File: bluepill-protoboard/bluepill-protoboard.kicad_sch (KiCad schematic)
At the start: 15 parts, among them J1 Conn_01x20_Socket, J10 Conn_01x04_Pin, J11 Conn_01x04_Pin, J13 Conn_01x06_Pin, J14 Conn_01x04_Pin, J15 Conn_01x04_Pin, J2 Conn_01x17_Pin, J3 Conn_01x17_Pin, J4 Conn_01x17_Pin, J5 Conn_01x04_Pin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

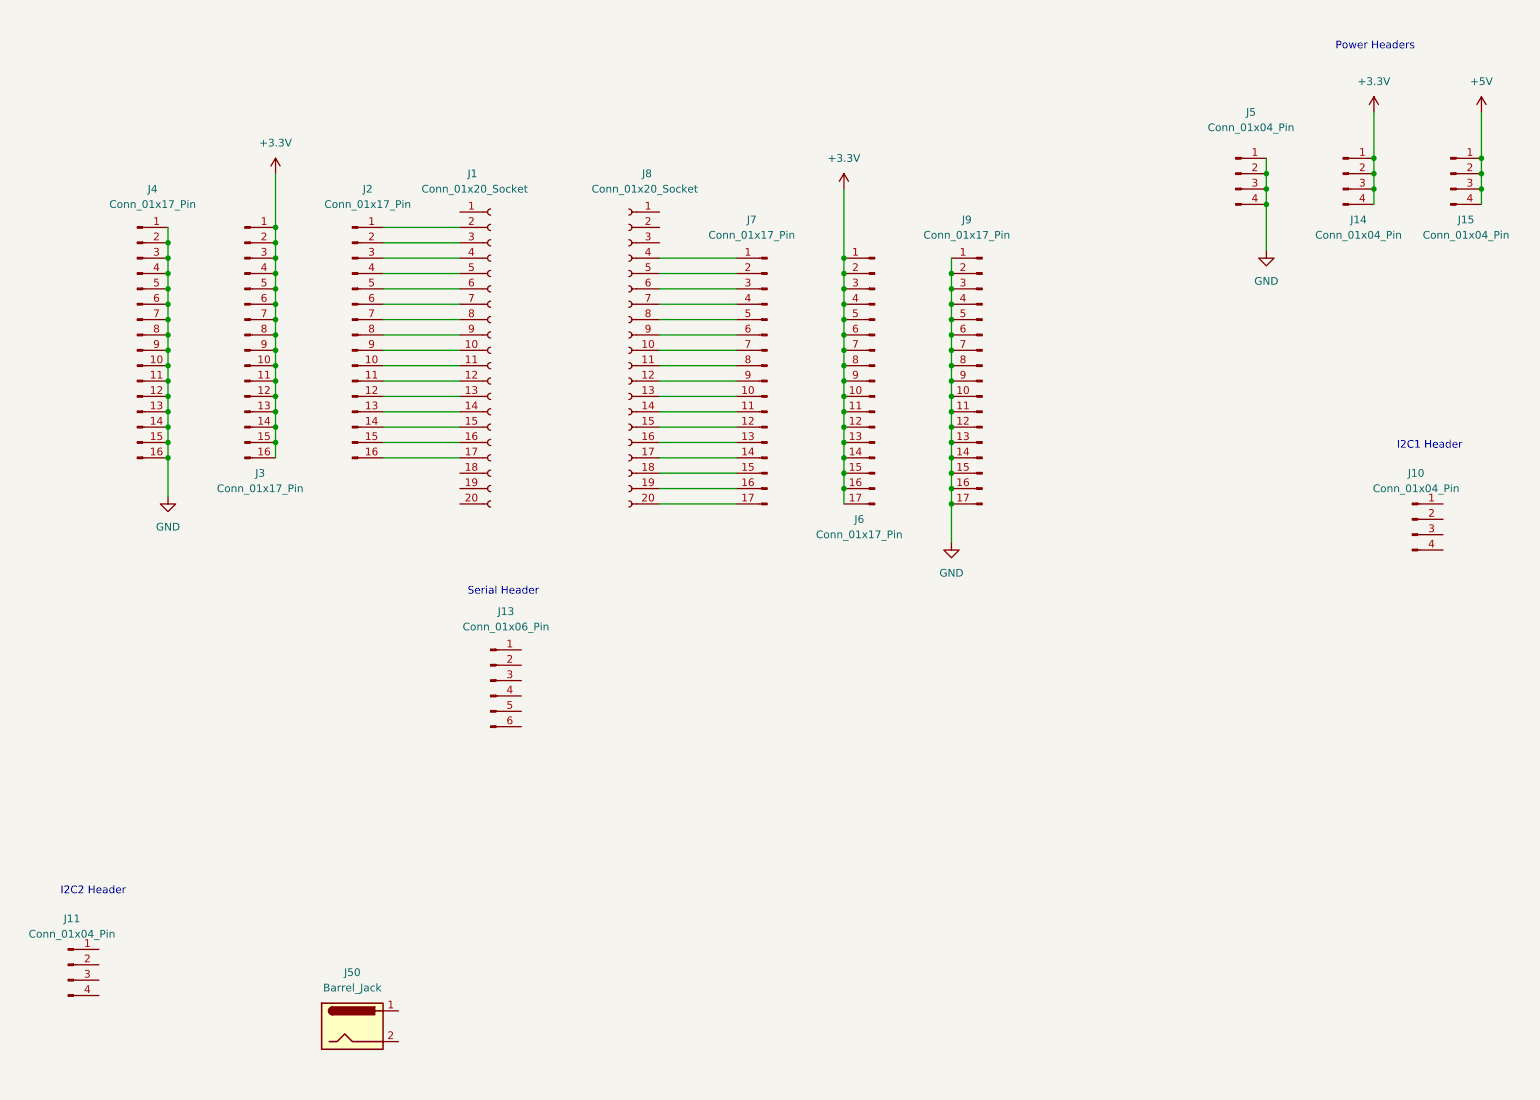
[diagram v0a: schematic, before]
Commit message: Headers done
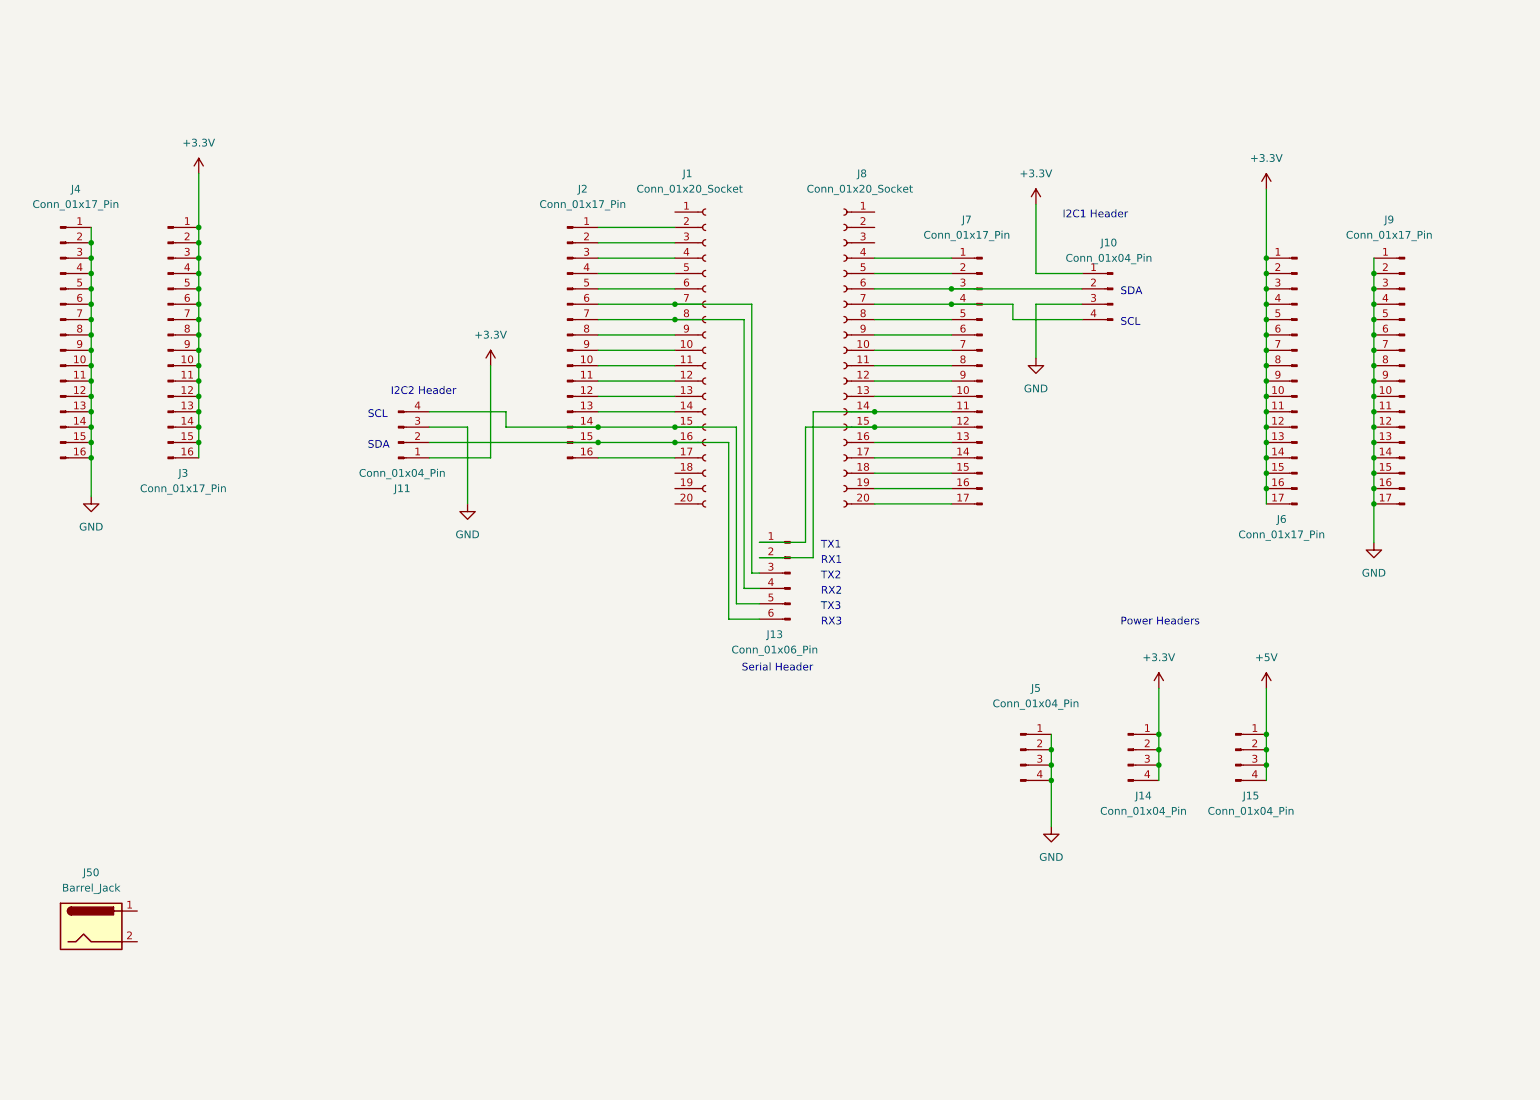
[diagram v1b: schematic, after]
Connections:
- net +3.3V: now also J10.1 (Pin_1), J11.1 (Pin_1)
- net GND: now also J10.3 (Pin_3), J11.3 (Pin_3)
- net at J1.15 (Pin_15), J2.14 (Pin_14): now also J11.4 (Pin_4), J13.5 (Pin_5)
- net at J1.16 (Pin_16), J2.15 (Pin_15): now also J11.2 (Pin_2), J13.6 (Pin_6)
- net at J1.7 (Pin_7), J2.6 (Pin_6): now also J13.3 (Pin_3)
- net at J1.8 (Pin_8), J2.7 (Pin_7): now also J13.4 (Pin_4)
- net at J10.2 (Pin_2): now also J7.3 (Pin_3), J8.6 (Pin_6)
- net at J10.4 (Pin_4): now also J7.4 (Pin_4), J8.7 (Pin_7)
- net at J7.11 (Pin_11), J8.14 (Pin_14): now also J13.2 (Pin_2)
- net at J7.12 (Pin_12), J8.15 (Pin_15): now also J13.1 (Pin_1)
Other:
- note added: "RX1"
- note added: "RX2"
- note added: "RX3"
- note added: "SCL"
- note added: "SDA"
- note added: "TX1"
- note added: "TX2"
- note added: "TX3"
- title: (none) -> Bluepill Protoboard
- moved on the sheet: J1, J10, J11, J13, J14, J15, J2, J3, J4, J5, J50, J6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

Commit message: Add license
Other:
- note added: "Licensed under GPL 3.0"
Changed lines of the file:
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@@
     (stroke (width 0) (type default))
+  )
+  (text "Licensed under GPL 3.0" (at 179.07 170.18 0)
+    (effects (font (size 1.27 1.27)) (justify left bottom))
   )
   (text "TX1" (at 152.4 102.87 0)

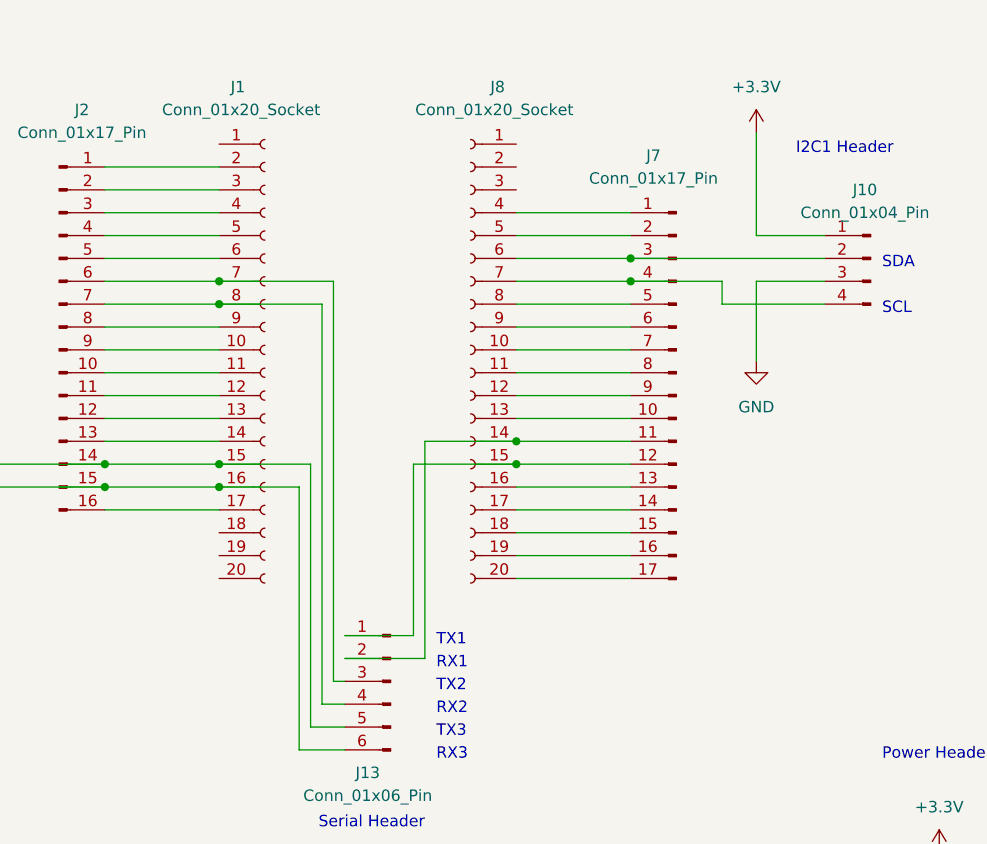
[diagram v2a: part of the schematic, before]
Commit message: Add pin labels
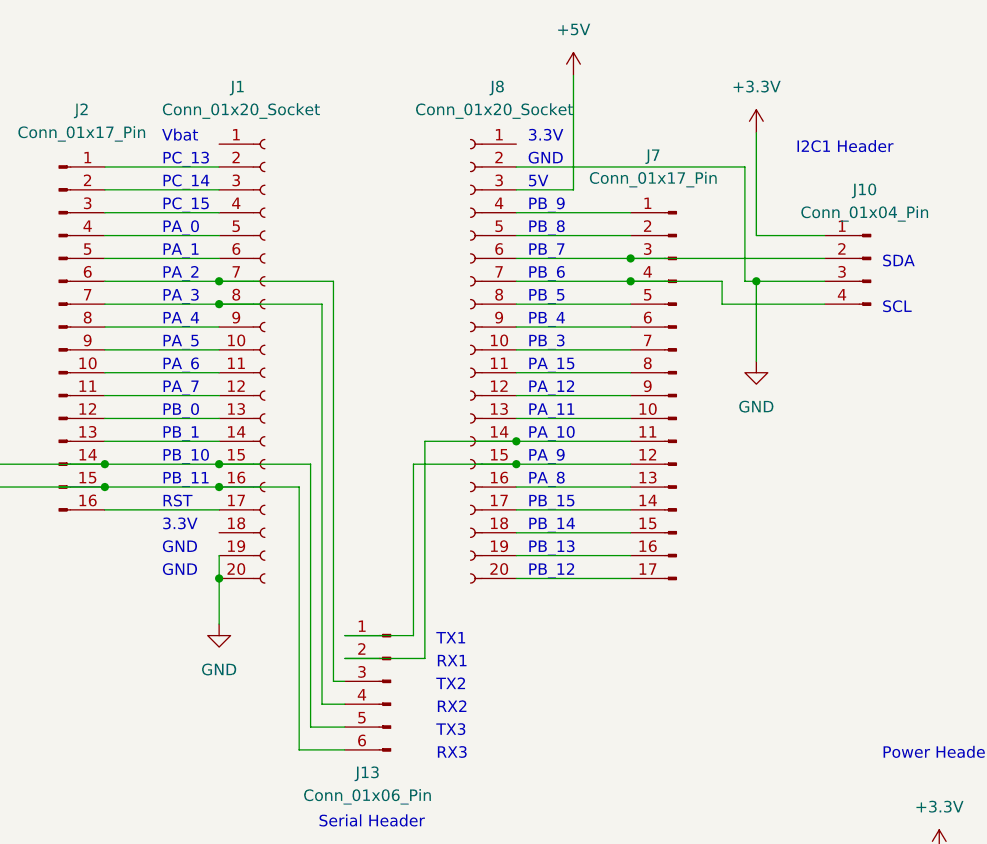
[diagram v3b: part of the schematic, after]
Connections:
- net +5V: now also J8.3 (Pin_3)
- net GND: now also J1.19 (Pin_19), J1.20 (Pin_20), J8.2 (Pin_2)
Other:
- note added: "3.3V"
- note added: "5V"
- note added: "GND"
- note added: "PA_0"
- note added: "PA_1"
- note added: "PA_10"
- note added: "PA_11"
- note added: "PA_12"
- note added: "PA_15"
- note added: "PA_2"
- note added: "PA_3"
- note added: "PA_4"
- note added: "PA_5"
- note added: "PA_6"
- note added: "PA_7"
- note added: "PA_8"
- note added: "PA_9"
- note added: "PB_0"
- note added: "PB_1"
- note added: "PB_10"
- note added: "PB_11"
- note added: "PB_12"
- note added: "PB_13"
- note added: "PB_14"
- note added: "PB_15"
- note added: "PB_3"
- note added: "PB_4"
- note added: "PB_5"
- note added: "PB_6"
- note added: "PB_7"
- note added: "PB_8"
- note added: "PB_9"
- note added: "PC_13"
- note added: "PC_14"
- note added: "PC_15"
- note added: "RST"
- note added: "Vbat"
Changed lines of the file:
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@@
   (junction (at 243.84 57.15) (diameter 0) (color 0 0 0 0)
   )
+  (junction (at 128.27 95.25) (diameter 0) (color 0 0 0 0)
+  )
   (junction (at 226.06 80.01) (diameter 0) (color 0 0 0 0)
   )
@@
   (junction (at 226.06 69.85) (diameter 0) (color 0 0 0 0)
   )
+  (junction (at 187.96 62.23) (diameter 0) (color 0 0 0 0)
+  )
   (junction (at 243.84 62.23) (diameter 0) (color 0 0 0 0)
   )
@@
     (stroke (width 0) (type default))
   )
+  (wire (pts (xy 187.96 62.23) (xy 195.58 62.23))
+    (stroke (width 0) (type default))
+  )
   (wire (pts (xy 31.75 77.47) (xy 31.75 80.01))
     (stroke (width 0) (type default))
@@
     (stroke (width 0) (type default))
   )
+  (wire (pts (xy 161.29 49.53) (xy 186.69 49.53))
+    (stroke (width 0) (type default))
+  )
   (wire (pts (xy 49.53 74.93) (xy 49.53 77.47))
     (stroke (width 0) (type default))
@@
     (stroke (width 0) (type default))
   )
+  (wire (pts (xy 128.27 95.25) (xy 128.27 100.33))
+    (stroke (width 0) (type default))
+  )
   (wire (pts (xy 149.86 82.55) (xy 161.29 82.55))
     (stroke (width 0) (type default))
@@
     (stroke (width 0) (type default))
   )
+  (wire (pts (xy 186.69 49.53) (xy 186.69 62.23))
+    (stroke (width 0) (type default))
+  )
   (wire (pts (xy 49.53 64.77) (xy 49.53 67.31))
     (stroke (width 0) (type default))
@@
     (stroke (width 0) (type default))
   )
+  (wire (pts (xy 161.29 52.07) (xy 167.64 52.07))
+    (stroke (width 0) (type default))
+  )
   (wire (pts (xy 31.75 62.23) (xy 31.75 64.77))
     (stroke (width 0) (type default))
@@
     (stroke (width 0) (type default))
   )
+  (wire (pts (xy 167.64 52.07) (xy 167.64 39.37))
+    (stroke (width 0) (type default))
+  )
   (wire (pts (xy 243.84 90.17) (xy 243.84 92.71))
     (stroke (width 0) (type default))
@@
     (stroke (width 0) (type default))
   )
-  (wire (pts (xy 195.58 62.23) (xy 187.96 62.23))
+  (wire (pts (xy 186.69 62.23) (xy 187.96 62.23))
     (stroke (width 0) (type default))
   )
@@
     (stroke (width 0) (type default))
   )
+  (wire (pts (xy 128.27 92.71) (xy 128.27 95.25))
+    (stroke (width 0) (type default))
+  )
   (wire (pts (xy 49.53 59.69) (xy 49.53 62.23))
     (stroke (width 0) (type default))
@@
     (effects (font (size 1.27 1.27)) (justify left bottom))
   )
+  (text "GND" (at 121.92 92.71 0)
+    (effects (font (size 1.27 1.27)) (justify left bottom))
+  )
+  (text "PC_15" (at 121.92 54.61 0)
+    (effects (font (size 1.27 1.27)) (justify left bottom))
+  )
   (text "TX1" (at 152.4 102.87 0)
     (effects (font (size 1.27 1.27)) (justify left bottom))
   )
+  (text "PA_1" (at 121.92 59.69 0)
+    (effects (font (size 1.27 1.27)) (justify left bottom))
+  )
+  (text "PA_6" (at 121.92 72.39 0)
+    (effects (font (size 1.27 1.27)) (justify left bottom))
+  )
+  (text "PB_10" (at 121.92 82.55 0)
+    (effects (font (size 1.27 1.27)) (justify left bottom))
+  )
+  (text "5V" (at 162.56 52.07 0)
+    (effects (font (size 1.27 1.27)) (justify left bottom))
+  )
+  (text "PA_5" (at 121.92 69.85 0)
+    (effects (font (size 1.27 1.27)) (justify left bottom))
+  )
+  (text "3.3V" (at 162.56 46.99 0)
+    (effects (font (size 1.27 1.27)) (justify left bottom))
+  )
+  (text "PA_8" (at 162.56 85.09 0)
+    (effects (font (size 1.27 1.27)) (justify left bottom))
+  )
   (text "RX2" (at 152.4 110.49 0)
     (effects (font (size 1.27 1.27)) (justify left bottom))
   )
+  (text "PB_11" (at 121.92 85.09 0)
+    (effects (font (size 1.27 1.27)) (justify left bottom))
+  )
   (text "RX3" (at 152.4 115.57 0)
     (effects (font (size 1.27 1.27)) (justify left bottom))
@@
     (effects (font (size 1.27 1.27)) (justify left bottom))
   )
+  (text "PB_8" (at 162.56 57.15 0)
+    (effects (font (size 1.27 1.27)) (justify left bottom))
+  )
+  (text "PB_14" (at 162.56 90.17 0)
+    (effects (font (size 1.27 1.27)) (justify left bottom))
+  )
+  (text "PB_5" (at 162.56 64.77 0)
+    (effects (font (size 1.27 1.27)) (justify left bottom))
+  )
+  (text "RST" (at 121.92 87.63 0)
+    (effects (font (size 1.27 1.27)) (justify left bottom))
+  )
+  (text "PA_10" (at 162.56 80.01 0)
+    (effects (font (size 1.27 1.27)) (justify left bottom))
+  )
+  (text "3.3V" (at 121.92 90.17 0)
+    (effects (font (size 1.27 1.27)) (justify left bottom))
+  )
+  (text "PA_12" (at 162.56 74.93 0)
+    (effects (font (size 1.27 1.27)) (justify left bottom))
+  )
   (text "SCL" (at 77.47 81.28 0)
     (effects (font (size 1.27 1.27)) (justify left bottom))
   )
+  (text "PA_0" (at 121.92 57.15 0)
+    (effects (font (size 1.27 1.27)) (justify left bottom))
+  )
+  (text "PA_15" (at 162.56 72.39 0)
+    (effects (font (size 1.27 1.27)) (justify left bottom))
+  )
+  (text "PA_11" (at 162.56 77.47 0)
+    (effects (font (size 1.27 1.27)) (justify left bottom))
+  )
   (text "SDA" (at 77.47 86.36 0)
     (effects (font (size 1.27 1.27)) (justify left bottom))
   )
+  (text "PB_4" (at 162.56 67.31 0)
+    (effects (font (size 1.27 1.27)) (justify left bottom))
+  )
+  (text "PC_14" (at 121.92 52.07 0)
+    (effects (font (size 1.27 1.27)) (justify left bottom))
+  )
+  (text "PC_13" (at 121.92 49.53 0)
+    (effects (font (size 1.27 1.27)) (justify left bottom))
+  )
+  (text "PB_7" (at 162.56 59.69 0)
+    (effects (font (size 1.27 1.27)) (justify left bottom))
+  )
   (text "I2C2 Header" (at 81.28 77.47 0)
+    (effects (font (size 1.27 1.27)) (justify left bottom))
+  )
+  (text "PA_7" (at 121.92 74.93 0)
+    (effects (font (size 1.27 1.27)) (justify left bottom))
+  )
+  (text "Vbat" (at 121.92 46.99 0)
     (effects (font (size 1.27 1.27)) (justify left bottom))
   )
@@
     (effects (font (size 1.27 1.27)) (justify right bottom))
   )
+  (text "PB_6" (at 162.56 62.23 0)
+    (effects (font (size 1.27 1.27)) (justify left bottom))
+  )
+  (text "PB_3" (at 162.56 69.85 0)
+    (effects (font (size 1.27 1.27)) (justify left bottom))
+  )
   (text "RX1" (at 152.4 105.41 0)
     (effects (font (size 1.27 1.27)) (justify left bottom))
   )
   (text "SDA" (at 201.93 60.96 0)
+    (effects (font (size 1.27 1.27)) (justify left bottom))
+  )
+  (text "PB_13" (at 162.56 92.71 0)
+    (effects (font (size 1.27 1.27)) (justify left bottom))
+  )
+  (text "PA_3" (at 121.92 64.77 0)
     (effects (font (size 1.27 1.27)) (justify left bottom))
   )
@@
     (effects (font (size 1.27 1.27)) (justify right bottom))
   )
+  (text "PB_15" (at 162.56 87.63 0)
+    (effects (font (size 1.27 1.27)) (justify left bottom))
+  )
+  (text "PB_0" (at 121.92 77.47 0)
+    (effects (font (size 1.27 1.27)) (justify left bottom))
+  )
   (text "TX3" (at 152.4 113.03 0)
     (effects (font (size 1.27 1.27)) (justify left bottom))
@@
     (effects (font (size 1.27 1.27)) (justify left bottom))
   )
+  (text "GND" (at 121.92 95.25 0)
+    (effects (font (size 1.27 1.27)) (justify left bottom))
+  )
+  (text "PA_9" (at 162.56 82.55 0)
+    (effects (font (size 1.27 1.27)) (justify left bottom))
+  )
+  (text "PB_12" (at 162.56 95.25 0)
+    (effects (font (size 1.27 1.27)) (justify left bottom))
+  )
+  (text "PB_1" (at 121.92 80.01 0)
+    (effects (font (size 1.27 1.27)) (justify left bottom))
+  )
   (text "SCL" (at 201.93 66.04 0)
+    (effects (font (size 1.27 1.27)) (justify left bottom))
+  )
+  (text "PA_4" (at 121.92 67.31 0)
+    (effects (font (size 1.27 1.27)) (justify left bottom))
+  )
+  (text "PB_9" (at 162.56 54.61 0)
+    (effects (font (size 1.27 1.27)) (justify left bottom))
+  )
+  (text "GND" (at 162.56 49.53 0)
+    (effects (font (size 1.27 1.27)) (justify left bottom))
+  )
+  (text "PA_2" (at 121.92 62.23 0)
     (effects (font (size 1.27 1.27)) (justify left bottom))
   )
@@
         )
       )
+    )
+  )
+  (symbol (lib_id "power:+5V") (at 167.64 39.37 0) (unit 1)
+    (in_bom yes) (on_board yes) (dnp no) (fields_autoplaced)
+    (property "Reference" "#PWR013" (at 167.64 43.18 0)
+      (effects (font (size 1.27 1.27)) hide)
+    )
+    (property "Value" "+5V" (at 167.64 34.29 0)
+      (effects (font (size 1.27 1.27)))
+    )
+    (property "Footprint" "" (at 167.64 39.37 0)
+      (effects (font (size 1.27 1.27)) hide)
+    )
+    (property "Datasheet" "" (at 167.64 39.37 0)
+      (effects (font (size 1.27 1.27)) hide)
+    )
+    (pin "1")
+    (instances
+      (project "bluepill-protoboard"
+        (path "/d234335a-6eb4-40d1-9f73-724446a9aca9"
+          (reference "#PWR013") (unit 1)
+        )
+      )
+    )
+  )
+  (symbol (lib_id "power:GND") (at 128.27 100.33 0) (unit 1)
+    (in_bom yes) (on_board yes) (dnp no) (fields_autoplaced)
+    (property "Reference" "#PWR012" (at 128.27 106.68 0)
+      (effects (font (size 1.27 1.27)) hide)
+    )
+    (property "Value" "GND" (at 128.27 105.41 0)
+      (effects (font (size 1.27 1.27)))
+    )
+    (property "Footprint" "" (at 128.27 100.33 0)
+      (effects (font (size 1.27 1.27)) hide)
+    )
+    (property "Datasheet" "" (at 128.27 100.33 0)
+      (effects (font (size 1.27 1.27)) hide)
+    )
+    (pin "1")
+    (instances
+      (project "bluepill-protoboard"
+        (path "/d234335a-6eb4-40d1-9f73-724446a9aca9"
+          (reference "#PWR012") (unit 1)
+        )
+      )
